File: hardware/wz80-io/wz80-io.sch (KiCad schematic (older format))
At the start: 22 parts, among them J1 CONN_01X04, J2 CONN_01X08, J3 CONN_01X32, SW1 SW_DIP_x08, U1 74LS245, U2 74LS595, U3 74LS374, U4 74LS374, U5 74LS374, U6 74LS138

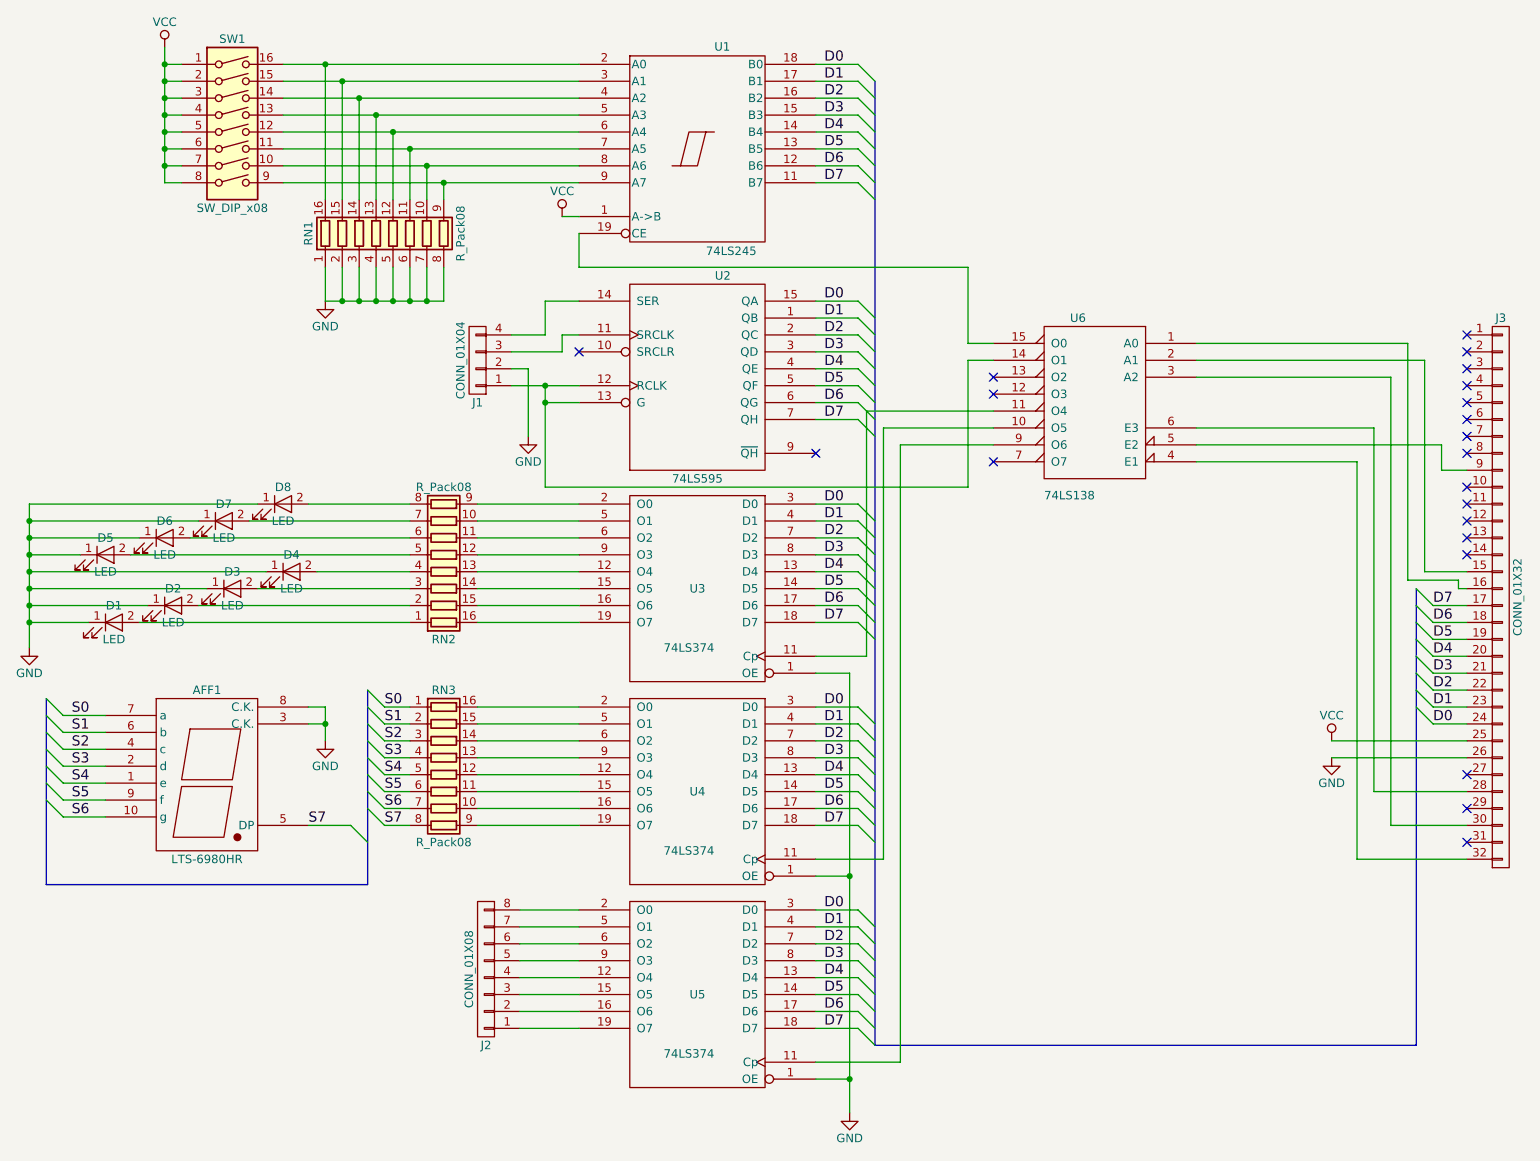
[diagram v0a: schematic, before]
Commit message: Moved schematics into hardware/. Added start of software.
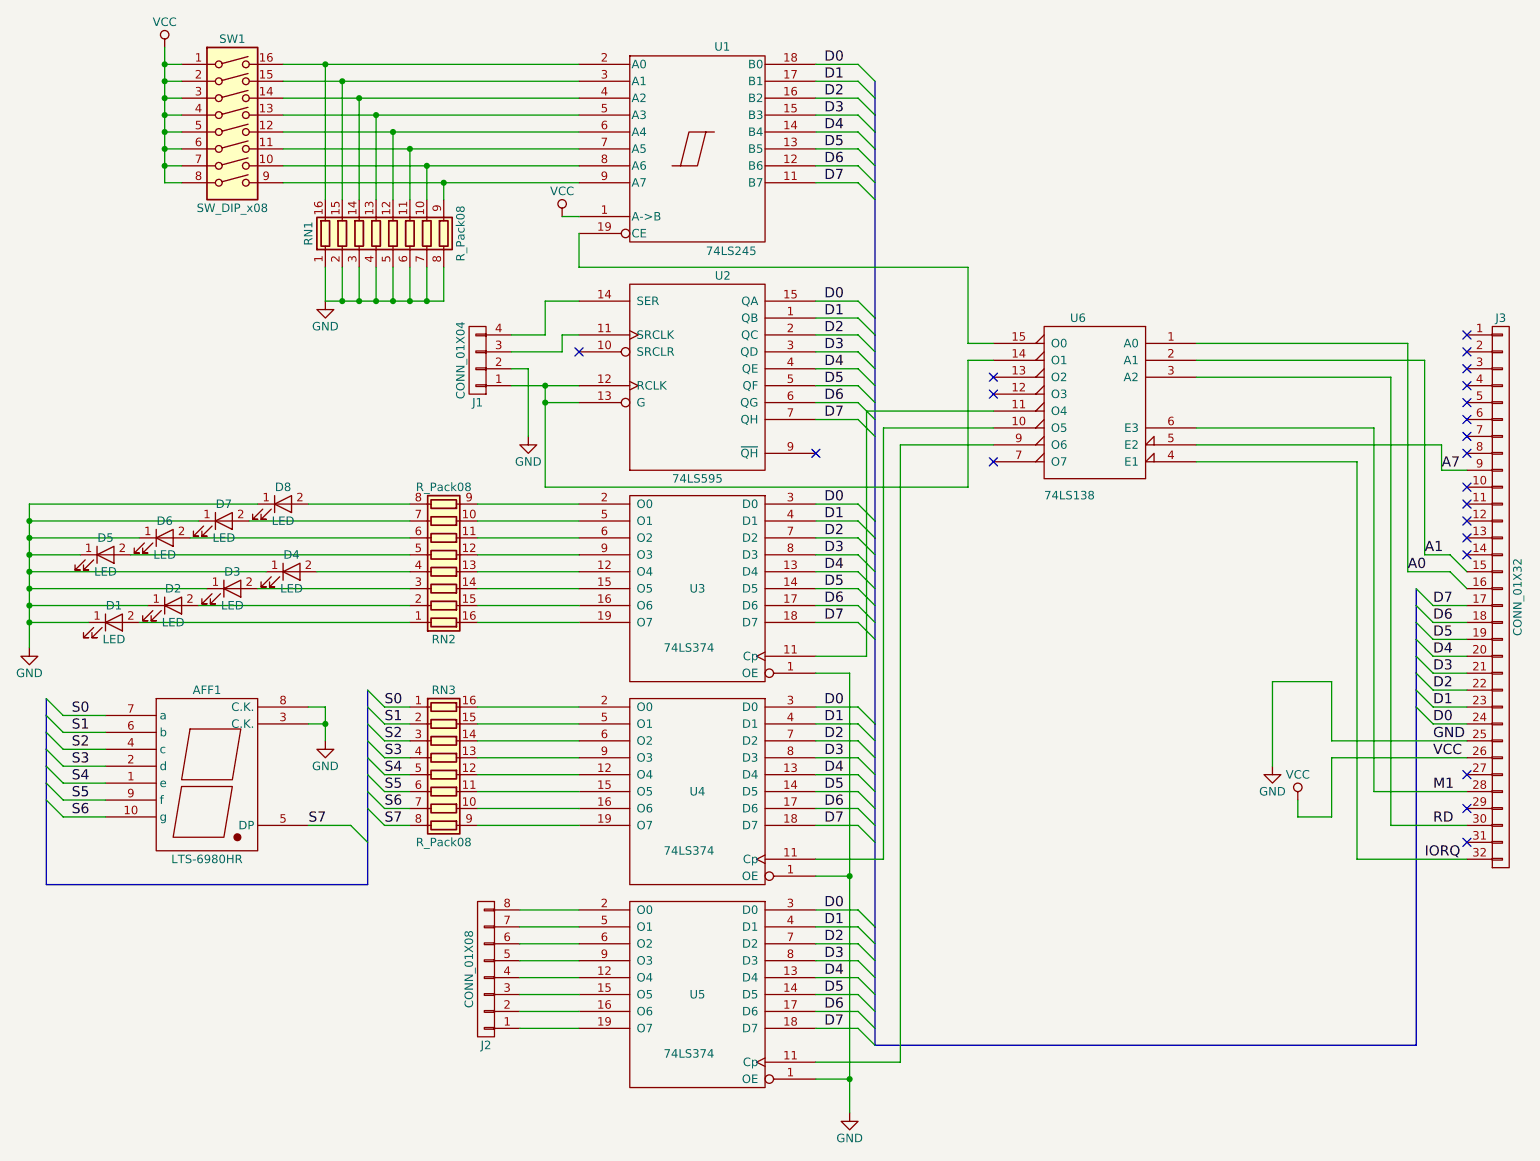
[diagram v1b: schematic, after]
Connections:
- net GND: now also J3.25 (P25); no longer J3.26 (P26)
- net VCC: now also J3.26 (P26); no longer J3.25 (P25)
- net A0: now reaches J3.16 (P16), U6.1 (A0)
- net A1: now reaches J3.15 (P15), U6.2 (A1)
- net RD: now reaches J3.30 (P30), U6.3 (A2)
- net IORQ: now reaches J3.32 (P32), U6.4 (E1)
- net A7: now reaches J3.9 (P9), U6.5 (E2)
- net M1: now reaches J3.28 (P28), U6.6 (E3)
